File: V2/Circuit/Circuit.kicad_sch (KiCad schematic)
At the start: 21 parts, among them J2 PinHeader-1x3, U1 TMC2209_SILENTSTEPSTICK, U2 LM338T

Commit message: further dev in BOM and schematics
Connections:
- net +24V: no longer R2.2, U2.2 (VOUT)
- net +5V: now reaches Encoder_Steps1.4 (Pin_4)
- net +5V: now also Encoder_Speed1.4 (Pin_4), R2.2, STC8H8K64U1.18 (Pin_18), U1.2 (VIO), U2.2 (VOUT)

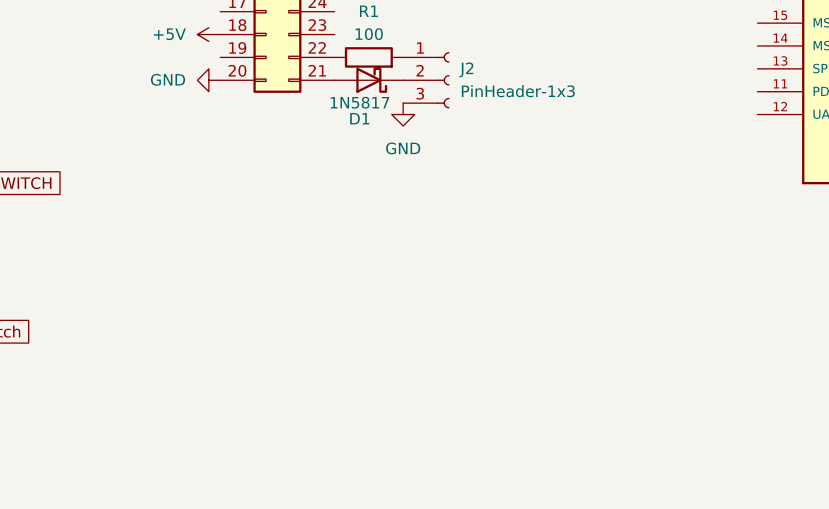
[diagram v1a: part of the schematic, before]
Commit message: added IDC connection for LCD and started programming, added gitignore and attribute
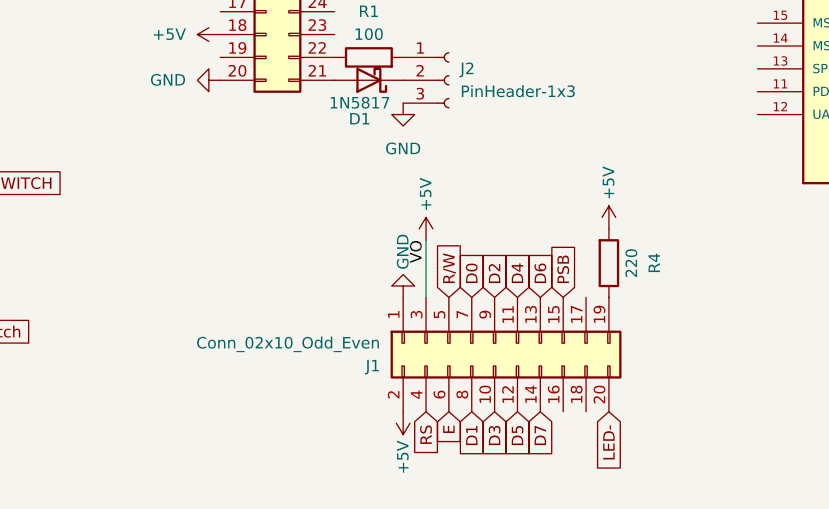
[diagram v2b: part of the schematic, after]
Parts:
- added J1: Conn_02x10_Odd_Even, Connector_IDC:IDC-Header_2x10_P2.54mm_Vertical, symbol Connector_Generic:Conn_02x10_Odd_Even
- added R4: 220, Resistor_THT:R_Axial_DIN0207_L6.3mm_D2.5mm_P7.62mm_Horizontal, symbol Device:R
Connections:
- net +5V: now also J1.2 (Pin_2), J1.3 (Pin_3), R4.2
- net GND: now also J1.1 (Pin_1)
- new net: J1.19 (Pin_19), R4.1
- new net D0: J1.7 (Pin_7)
- new net D1: J1.8 (Pin_8)
- new net D2: J1.9 (Pin_9)
- new net D3: J1.10 (Pin_10)
- new net D4: J1.11 (Pin_11)
- new net D5: J1.12 (Pin_12)
- new net D6: J1.13 (Pin_13)
- new net D7: J1.14 (Pin_14)
- new net E: J1.6 (Pin_6)
- new net LED-: J1.20 (Pin_20)
- new net PSB: J1.15 (Pin_15)
- new net RS: J1.4 (Pin_4)
- new net R/W: J1.5 (Pin_5)

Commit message: added control mode switch
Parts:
- added Control-mode-switch: JST-2P, Connector_JST:JST_EH_B2B-EH-A_1x02_P2.50mm_Vertical, symbol Connector_Generic:Conn_01x02
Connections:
- net GND: now also Control-mode-switch.1 (Pin_1)
- new net control-mode-switch: Control-mode-switch.2 (Pin_2)
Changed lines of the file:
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@@
 		)
 	)
+	(global_label "control-mode-switch"
+		(shape input)
+		(at 91.44 160.02 0)
+		(fields_autoplaced yes)
+		(effects
+			(font
+				(size 1.27 1.27)
+			)
+			(justify left)
+		)
+		(property "Intersheetrefs" "${INTERSHEET_REFS}"
+			(at 115.2893 160.02 0)
+			(effects
+				(font
+					(size 1.27 1.27)
+				)
+				(justify left)
+				(hide yes)
+			)
+		)
+	)
 	(global_label "D3"
 		(shape input)
@@
 	)
 	(symbol
+		(lib_id "power:GND")
+		(at 91.44 162.56 90)
+		(unit 1)
+		(exclude_from_sim no)
+		(in_bom yes)
+		(on_board yes)
+		(dnp no)
+		(fields_autoplaced yes)
+		(property "Reference" "#PWR029"
+			(at 97.79 162.56 0)
+			(effects
+				(font
+					(size 1.27 1.27)
+				)
+				(hide yes)
+			)
+		)
+		(property "Value" "GND"
+			(at 95.25 162.5599 90)
+			(effects
+				(font
+					(size 1.27 1.27)
+				)
+				(justify right)
+			)
+		)
+		(property "Footprint" ""
+			(at 91.44 162.56 0)
+			(effects
+				(font
+					(size 1.27 1.27)
+				)
+				(hide yes)
+			)
+		)
+		(property "Datasheet" ""
+			(at 91.44 162.56 0)
+			(effects
+				(font
+					(size 1.27 1.27)
+				)
+				(hide yes)
+			)
+		)
+		(property "Description" "Power symbol creates a global label with name \"GND\" , ground"
+			(at 91.44 162.56 0)
+			(effects
+				(font
+					(size 1.27 1.27)
+				)
+				(hide yes)
+			)
+		)
+		(pin "1"
+		)
+		(instances
+			(project "Circuit"
+				(path "/b31af398-847c-4559-8133-d2c3ef6f7d2e"
+					(reference "#PWR029")
+					(unit 1)
+				)
+			)
+		)
+	)
+	(symbol
 		(lib_id "Connector_Generic:Conn_01x05")
 		(at 86.36 54.61 0)
@@
 					(unit 1)
 				)
+			)
+		)
+	)
+	(symbol
+		(lib_id "Connector_Generic:Conn_01x02")
+		(at 86.36 162.56 180)
+		(unit 1)
+		(exclude_from_sim no)
+		(in_bom yes)
+		(on_board yes)
+		(dnp no)
+		(fields_autoplaced yes)
+		(property "Reference" "Control-mode-switch"
+			(at 86.36 153.67 0)
+			(effects
+				(font
+					(size 1.27 1.27)
+				)
+			)
+		)
+		(property "Value" "JST-2P"
+			(at 86.36 156.21 0)
+			(effects
+				(font
+					(size 1.27 1.27)
+				)
+			)
+		)
+		(property "Footprint" "Connector_JST:JST_EH_B2B-EH-A_1x02_P2.50mm_Vertical"
+			(at 86.36 162.56 0)
+			(effects
+				(font
+					(size 1.27 1.27)
+				)
+				(hide yes)
+			)
+		)
+		(property "Datasheet" "~"
+			(at 86.36 162.56 0)
+			(effects
+				(font
+					(size 1.27 1.27)
+				)
+				(hide yes)
+			)
+		)
+		(property "Description" "Generic connector, single row, 01x02, script generated (kicad-library-utils/schlib/autogen/connector/)"
+			(at 86.36 162.56 0)
+			(effects
+				(font
+					(size 1.27 1.27)
+				)
+				(hide yes)
+			)
+		)
+		(pin "2"
+		)
+		(pin "1"
+		)
+		(instances
+			(project "Circuit"
+				(path "/b31af398-847c-4559-8133-d2c3ef6f7d2e"
+					(reference "Control-mode-switch")
+					(unit 1)
+				)

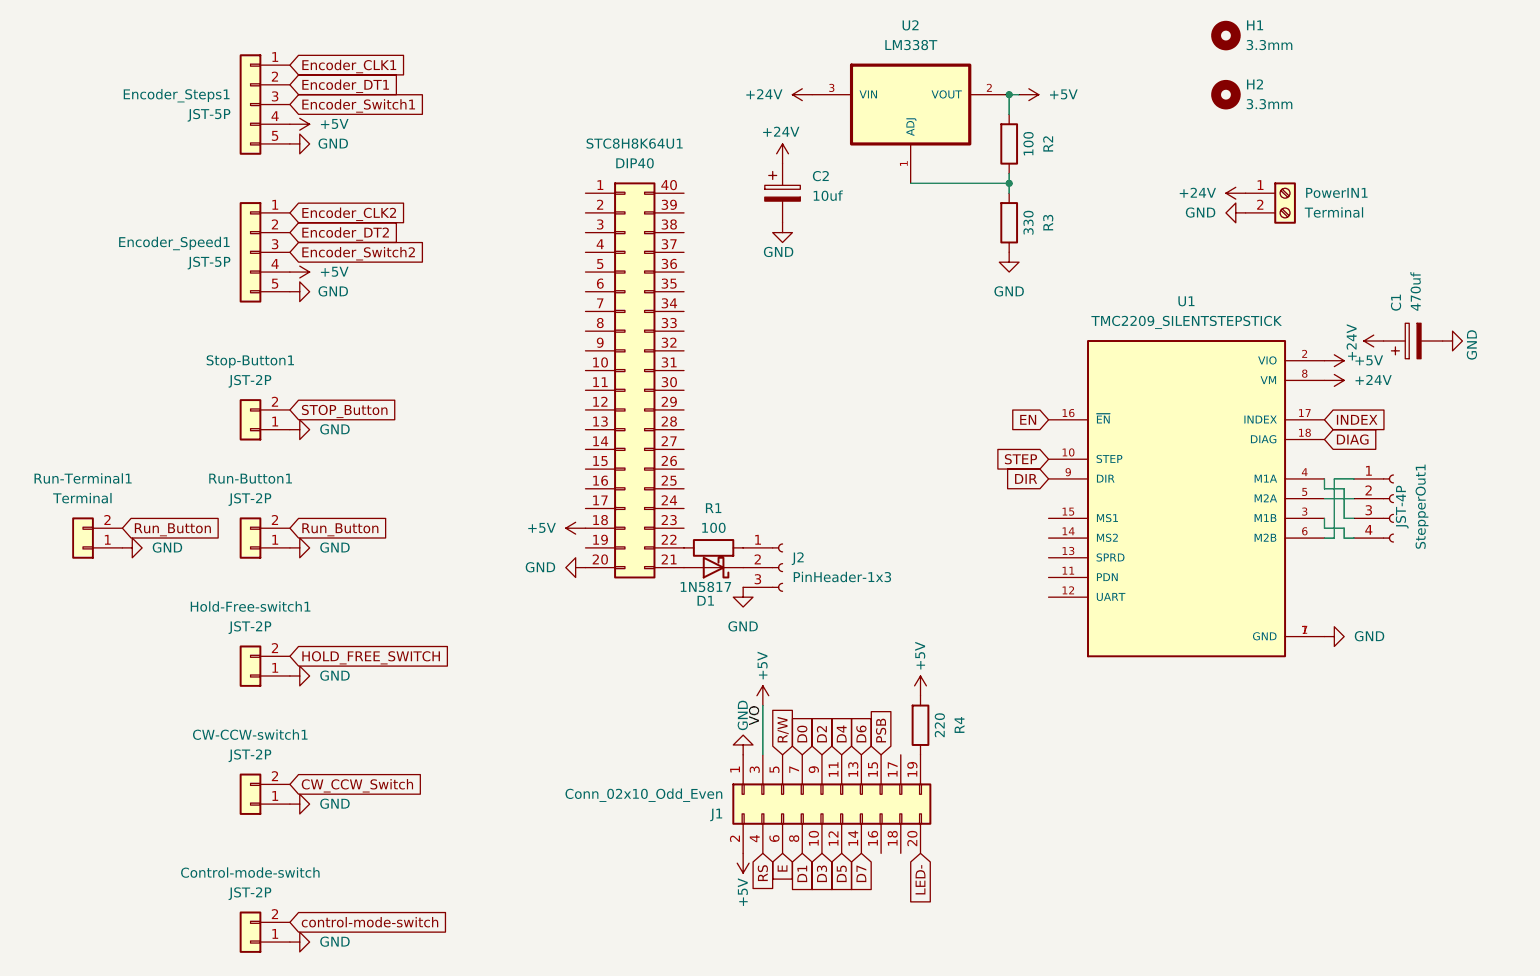
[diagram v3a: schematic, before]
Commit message: changed main MCU and started Programming
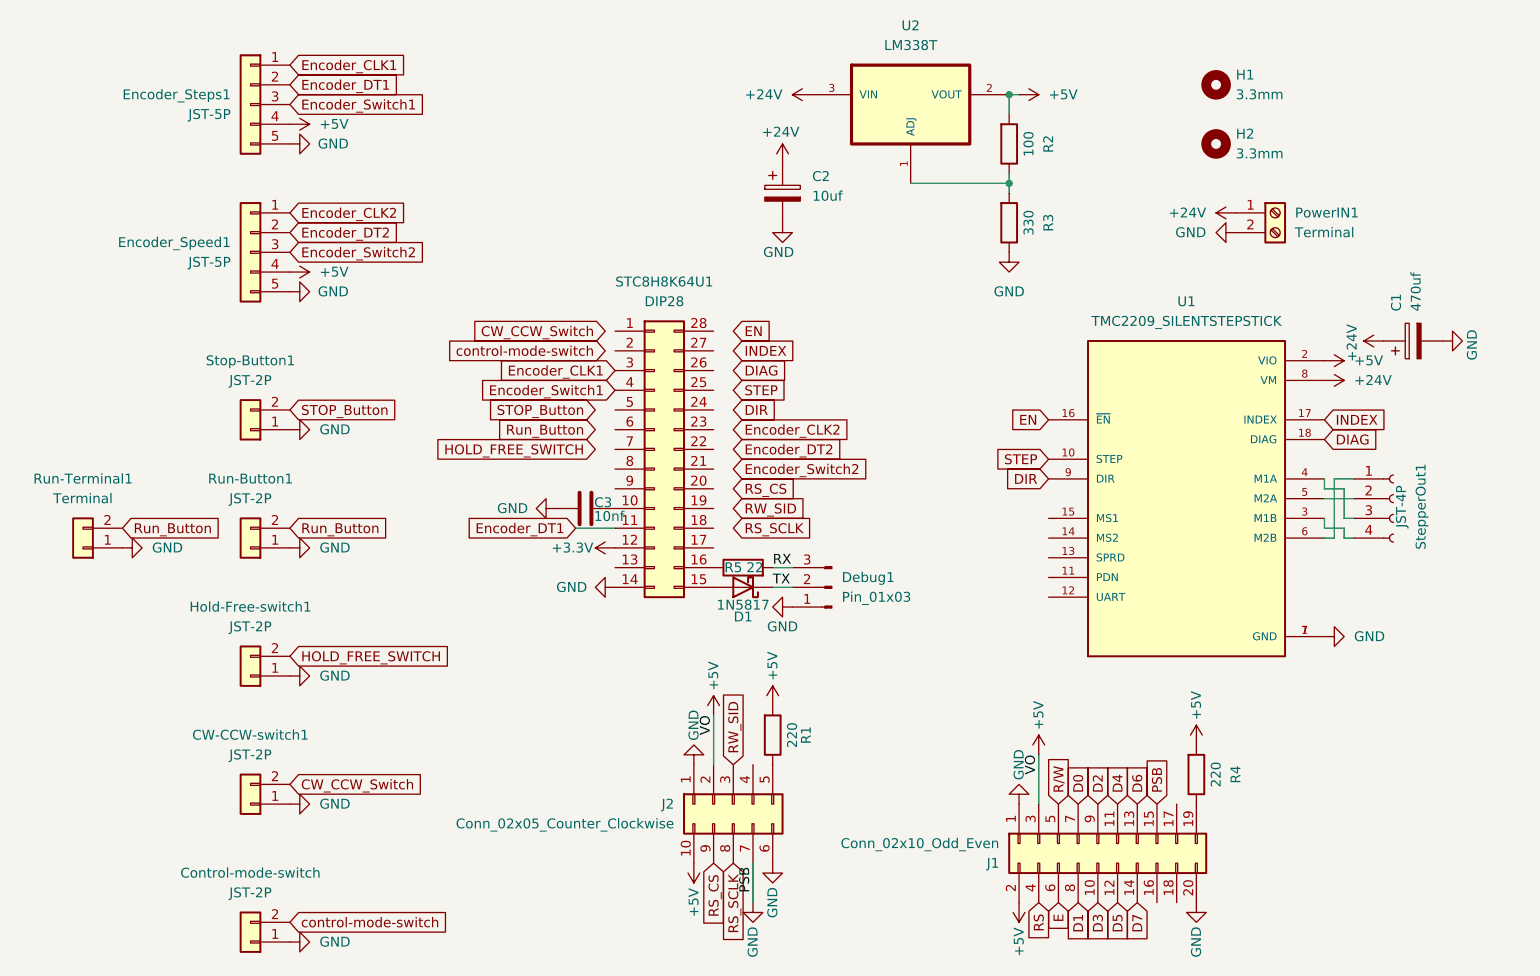
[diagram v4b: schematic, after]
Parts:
- removed J2: PinHeader-1x3, Connector_PinHeader_2.54mm:PinHeader_1x03_P2.54mm_Vertical, symbol Connector:Conn_01x03_Socket
- removed STC8H8K64U1: DIP40, Package_DIP:DIP-40_W15.24mm_LongPads, symbol Connector_Generic:Conn_02x20_Counter_Clockwise
- added C3: 10nf, Resistor_THT:R_Axial_DIN0207_L6.3mm_D2.5mm_P7.62mm_Horizontal, symbol Device:C
- added Debug1: Pin_01x03, Connector_PinHeader_2.54mm:PinHeader_1x03_P2.54mm_Vertical, symbol Connector:Conn_01x03_Pin
- added J2: Conn_02x05_Counter_Clockwise, Connector_IDC:IDC-Header_2x05_P2.54mm_Vertical, symbol Connector_Generic:Conn_02x05_Counter_Clockwise
- added R5: 22, Resistor_THT:R_Axial_DIN0207_L6.3mm_D2.5mm_P7.62mm_Horizontal, symbol Device:R
- added STC8H8K64U1: DIP28, Package_DIP:DIP-28_W7.62mm_Socket_LongPads, symbol Connector_Generic:Conn_02x14_Counter_Clockwise
- R1: value 100 -> 220
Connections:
- net LED- is gone; now on net GND: J1.20 (Pin_20)
- net PSB is gone; now on net GND: J1.15 (Pin_15)
- net +5V: now also R1.2, J2.10 (Pin_10), J2.2 (Pin_2)
- net Encoder_CLK1: now also STC8H8K64U1.3 (Pin_3)
- net Encoder_DT1: now also STC8H8K64U1.11 (Pin_11)
- net Encoder_Switch1: now also STC8H8K64U1.4 (Pin_4)
- net GND: now also C3.1, Debug1.1 (Pin_1), J2.1 (Pin_1), J2.6 (Pin_6), J2.7 (Pin_7), STC8H8K64U1.14 (Pin_14)
- net at R1.1: now also J2.5 (Pin_5)
- net at D1.2 (A): now also STC8H8K64U1.15 (Pin_15)
- net TX: now reaches D1.1 (K)
- net TX: now also Debug1.2 (Pin_2)
- new net: C3.2, STC8H8K64U1.10 (Pin_10)
- new net: R5.1, STC8H8K64U1.16 (Pin_16)
- new net +3.3V: STC8H8K64U1.12 (Pin_12)
- new net RS_CS: J2.9 (Pin_9)
- new net RS_SCLK: J2.8 (Pin_8)
- new net RW_SID: J2.3 (Pin_3)
- new net RX: Debug1.3 (Pin_3), R5.2
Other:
- moved on the sheet: H1, H2, J1, PowerIN1, R4

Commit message: finished pin mapping and most of HAL layer Programming
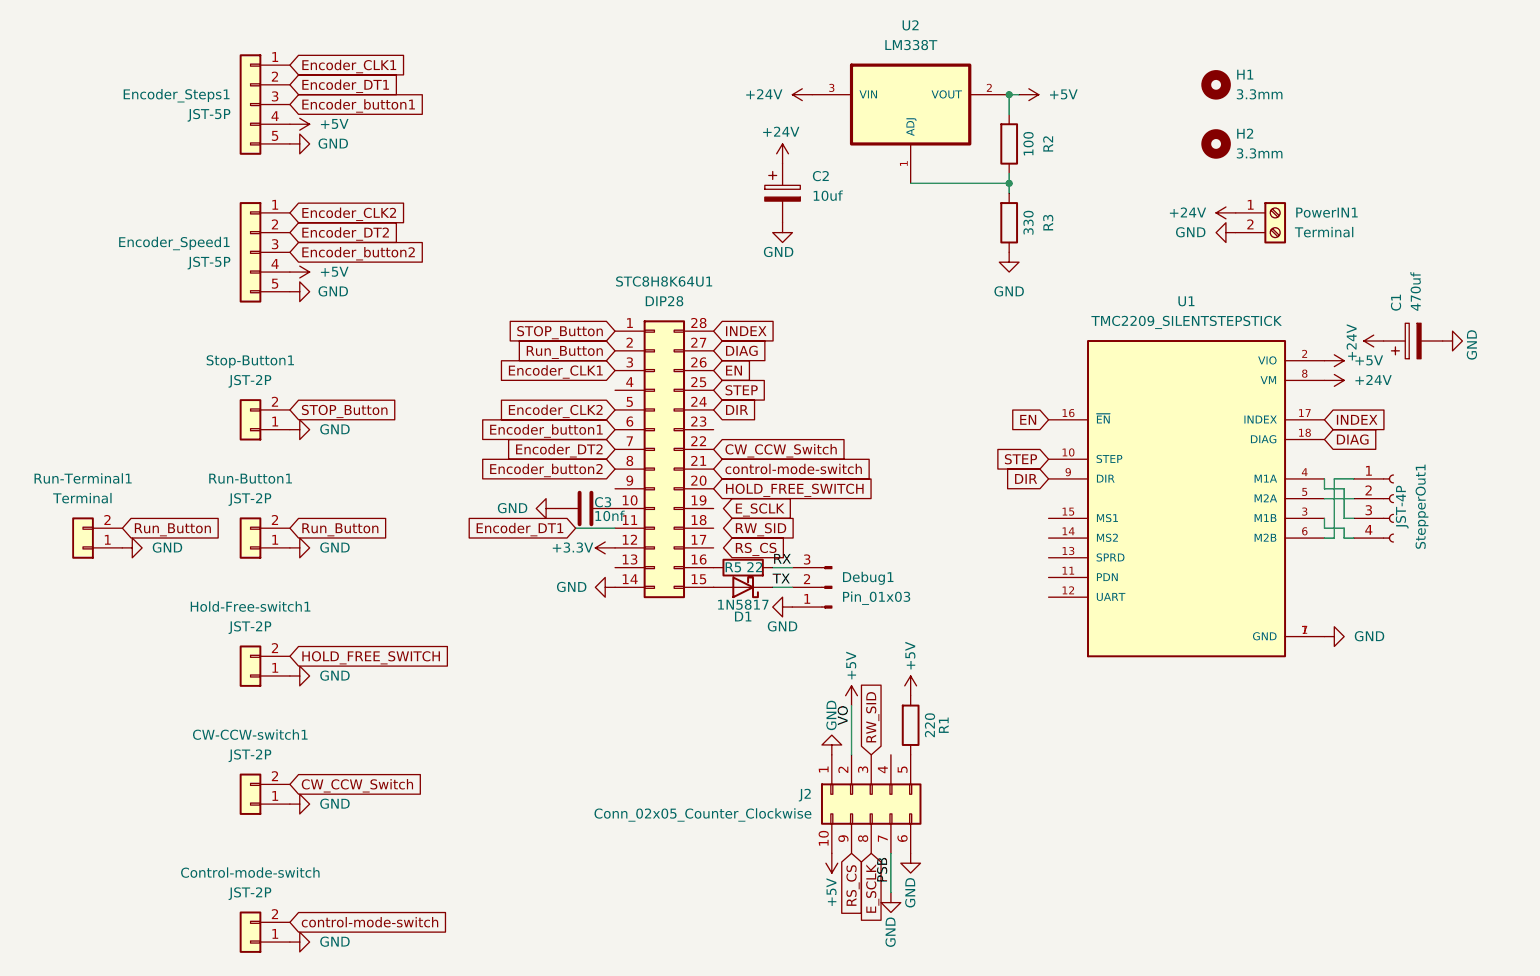
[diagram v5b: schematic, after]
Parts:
- removed J1: Conn_02x10_Odd_Even, Connector_IDC:IDC-Header_2x10_P2.54mm_Vertical, symbol Connector_Generic:Conn_02x10_Odd_Even
- removed R4: 220, Resistor_THT:R_Axial_DIN0207_L6.3mm_D2.5mm_P7.62mm_Horizontal, symbol Device:R
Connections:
- net Encoder_Switch2 is gone; now on net Encoder_button2: Encoder_Speed1.3 (Pin_3)
- net CW_CCW_Switch: now also STC8H8K64U1.22 (Pin_22)
- net DIAG: now also STC8H8K64U1.27 (Pin_27)
- net DIR: now also STC8H8K64U1.24 (Pin_24)
- net EN: now also STC8H8K64U1.26 (Pin_26)
- net Encoder_CLK2: now also STC8H8K64U1.5 (Pin_5)
- net Encoder_DT2: now also STC8H8K64U1.7 (Pin_7)
- net HOLD_FREE_SWITCH: now also STC8H8K64U1.20 (Pin_20)
- net INDEX: now also STC8H8K64U1.28 (Pin_28)
- net Run_Button: now also STC8H8K64U1.2 (Pin_2)
- net STEP: now also STC8H8K64U1.25 (Pin_25)
- net STOP_Button: now also STC8H8K64U1.1 (Pin_1)
- net control-mode-switch: now also STC8H8K64U1.21 (Pin_21)
- net Encoder_button1: now reaches STC8H8K64U1.6 (Pin_6)
- net Encoder_button1: now also Encoder_Steps1.3 (Pin_3)
- net Encoder_button2: now reaches STC8H8K64U1.8 (Pin_8)
- net Encoder_Switch1: no longer names the net of STC8H8K64U1.4 (Pin_4)
- net Encoder_Switch1: no longer Encoder_Steps1.3 (Pin_3)
- net RS_SCLK renamed E_SCLK
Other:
- moved on the sheet: J2, R1

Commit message: Finshed all HAL and a good chunk of application layer, finalized circuit schematic
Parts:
- C2: footprint Capacitor_THT:CP_Radial_D8.0mm_P3.50mm -> Capacitor_THT:CP_Radial_D5.0mm_P2.50mm
- CW-CCW-switch1, Hold-Free-switch1, Run-Button1, Stop-Button1: value JST-2P -> JST2P
- Control-mode-switch1: renamed from Control-mode-switch; value JST-2P -> JST2P
- Encoder1: renamed from Encoder_Steps1; value JST-5P -> JST5P
- Encoder2: renamed from Encoder_Speed1; value JST-5P -> JST5P
- J2: value Conn_02x05_Counter_Clockwise -> IDC-10P
- PowerIN1: footprint (none) -> TerminalBlock:TerminalBlock_bornier-2_P5.08mm
- R2: value 100 -> 200
- R5: value 22 -> 100
- StepperOut1: value JST-4P -> JST4P
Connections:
- net CW_CCW_Switch: now also CW-CCW-switch1.1 (Pin_1); no longer CW-CCW-switch1.2 (Pin_2)
- net DIAG: now also STC8H8K64U1.7 (Pin_7); no longer STC8H8K64U1.27 (Pin_27)
- net DIR: now also STC8H8K64U1.4 (Pin_4); no longer STC8H8K64U1.24 (Pin_24)
- net EN: now also STC8H8K64U1.6 (Pin_6); no longer STC8H8K64U1.26 (Pin_26)
- net E_SCLK: now also STC8H8K64U1.28 (Pin_28)
- net Encoder_CLK2: now also STC8H8K64U1.23 (Pin_23); no longer STC8H8K64U1.5 (Pin_5)
- net Encoder_DT2: now also STC8H8K64U1.24 (Pin_24); no longer STC8H8K64U1.7 (Pin_7)
- net Encoder_button1: now also STC8H8K64U1.17 (Pin_17); no longer STC8H8K64U1.6 (Pin_6)
- net Encoder_button2: now also STC8H8K64U1.25 (Pin_25); no longer STC8H8K64U1.8 (Pin_8)
- net GND: now also CW-CCW-switch1.2 (Pin_2), Control-mode-switch1.2 (Pin_2), Hold-Free-switch1.2 (Pin_2), Run-Button1.2 (Pin_2), Run-Terminal1.2 (Pin_2), STC8H8K64U1.13 (Pin_13), Stop-Button1.2 (Pin_2), U1.13 (SPRD), U1.14 (MS2), U1.15 (MS1); no longer CW-CCW-switch1.1 (Pin_1), Control-mode-switch1.1 (Pin_1), Hold-Free-switch1.1 (Pin_1), Run-Button1.1 (Pin_1), Run-Terminal1.1 (Pin_1), Stop-Button1.1 (Pin_1)
- net HOLD_FREE_SWITCH: now also Hold-Free-switch1.1 (Pin_1); no longer Hold-Free-switch1.2 (Pin_2)
- net INDEX: now also STC8H8K64U1.8 (Pin_8); no longer STC8H8K64U1.28 (Pin_28)
- net RS_CS: now also STC8H8K64U1.26 (Pin_26)
- net RW_SID: now also STC8H8K64U1.27 (Pin_27)
- net Run_Button: now also Run-Button1.1 (Pin_1), Run-Terminal1.1 (Pin_1), STC8H8K64U1.18 (Pin_18); no longer Run-Button1.2 (Pin_2), Run-Terminal1.2 (Pin_2), STC8H8K64U1.2 (Pin_2)
- net STEP: now also STC8H8K64U1.5 (Pin_5); no longer STC8H8K64U1.25 (Pin_25)
- net STOP_Button: now also STC8H8K64U1.19 (Pin_19), Stop-Button1.1 (Pin_1); no longer STC8H8K64U1.1 (Pin_1), Stop-Button1.2 (Pin_2)
- net control-mode-switch: now also Control-mode-switch1.1 (Pin_1); no longer Control-mode-switch1.2 (Pin_2)
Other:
- moved on the sheet: C1, CW-CCW-switch1, Control-mode-switch1, Encoder1, Encoder2, Hold-Free-switch1, Run-Button1, Run-Terminal1, Stop-Button1

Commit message: almost finished pcb tracing
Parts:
- removed J2: IDC-10P, Connector_IDC:IDC-Header_2x05_P2.54mm_Vertical, symbol Connector_Generic:Conn_02x05_Counter_Clockwise
- added J1: Conn_02x05_Odd_Even, Connector_IDC:IDC-Header_2x05_P2.54mm_Vertical, symbol Connector_Generic:Conn_02x05_Odd_Even
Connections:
- net +3.3V is gone; now on net +5V: STC8H8K64U1.12 (Pin_12)
- net E_SCLK: now also J1.1 (Pin_1)
- net RS_CS: now also J1.5 (Pin_5)
- net RW_SID: now also J1.3 (Pin_3)
- net at R1.1: now also J1.10 (Pin_10)
